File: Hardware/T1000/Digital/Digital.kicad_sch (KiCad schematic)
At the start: 71 parts, among them J1 Conn_01x02_Pin, J2 Conn_01x06_Socket, J3 Conn_01x04_Pin, J4 FTSH-107-01-L-DV-K-A, J5 USB_C_Receptacle_USB2.0, SW1 SW_SPDT, SW2 SW_SPDT, U1 MS5607-02BA, U2 MIA-M10Q, U3 STM32L422TBYx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

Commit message: V0 changes before order
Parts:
- removed BT1: 1S, Connector_JST:JST_PH_S2B-PH-K_1x02_P2.00mm_Horizontal, symbol Device:Battery_Cell
- removed C16, C17, C21: 1uF, Capacitor_SMD:C_0603_1608Metric, symbol Device:C_Small
- removed C18, C22, C23: 10uF, Capacitor_SMD:C_0805_2012Metric, symbol Device:C_Small
- removed C19: 2.2pF, Capacitor_SMD:C_0402_1005Metric, symbol Device:C_Small
- removed C20: 15uF, Capacitor_SMD:C_1206_3216Metric, symbol Device:C_Small
- removed D2: LED_Small, LED_SMD:LED_0603_1608Metric, symbol Device:LED_Small
- removed L1: 1uH, Inductor_SMD:L_0805_2012Metric, symbol Device:L_Small
- removed L2: 3.3uH, Inductor_SMD:L_1210_3225Metric, symbol Device:L_Small
- removed R11: 100m, Resistor_SMD:R_0402_1005Metric, symbol Device:R_Small
- removed R12: 10k, Resistor_SMD:R_0402_1005Metric, symbol Device:R_Small
- removed R13: 649k, Resistor_SMD:R_0402_1005Metric, symbol Device:R_Small
- removed R14: 294k, Resistor_SMD:R_0402_1005Metric, symbol Device:R_Small
- removed R15, R20: ??, Resistor_SMD:R_0402_1005Metric, symbol Device:R_Small
- removed R16, R19: 100k, Resistor_SMD:R_0402_1005Metric, symbol Device:R_Small
- removed R17: 113k, Resistor_SMD:R_0402_1005Metric, symbol Device:R_Small
- removed R18: 0, Resistor_SMD:R_0402_1005Metric, symbol Device:R_Small
- removed TP3: TestPoint, TestPoint:TestPoint_Pad_D1.0mm, symbol Connector:TestPoint
- removed U5: MIC5504-3.3YM5, Package_TO_SOT_SMD:SOT-23-5, symbol Regulator_Linear:MIC5504-3.3YM5
- removed U6: LM66200DRLR, BPP_Lib:SOT-5X3_DRL_TEX, symbol BPP_Lib:LM66200DRLR
- removed U7: LTC4065EDC-TRMPBF, BPP_Lib:DFN-6_DC_LIT, symbol BPP_Lib:LTC4065AEDC-TRMPBF
- removed U8: LTC3306CACBZ-R7, BPP_Lib:CB-6-19_ADI, symbol BPP_Lib:LTC3306CACBZ-R7
- added H1, H2: MountingHole, MountingHole:MountingHole_2.2mm_M2, symbol Mechanical:MountingHole
- added R24: 51k, Resistor_SMD:R_0402_1005Metric, symbol Device:R_Small
- J1: footprint Connector_PinHeader_1.00mm:PinHeader_1x02_P1.00mm_Vertical -> Connector_PinHeader_2.54mm:PinHeader_1x02_P2.54mm_Vertical
- Y2: value Crystal_Small -> 32.768k
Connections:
- net COMP1_INP: now also R24.2
- net VDD: now also R24.1
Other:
- added sheet Power (power.kicad_sch)
- note added: "Cutdown -> COMP1 is open drain, so pull up required"
- note removed: "1.8V SMPS"
- note removed: "3.3V SMPS"
- note removed: "Battery Charger"
- note removed: "Ideal Diode OR"
- company: (none) -> UMDBPP
- title: (none) -> T1000 - Digital & RF
- moved on the sheet: C15, J2, J3, J4, R8

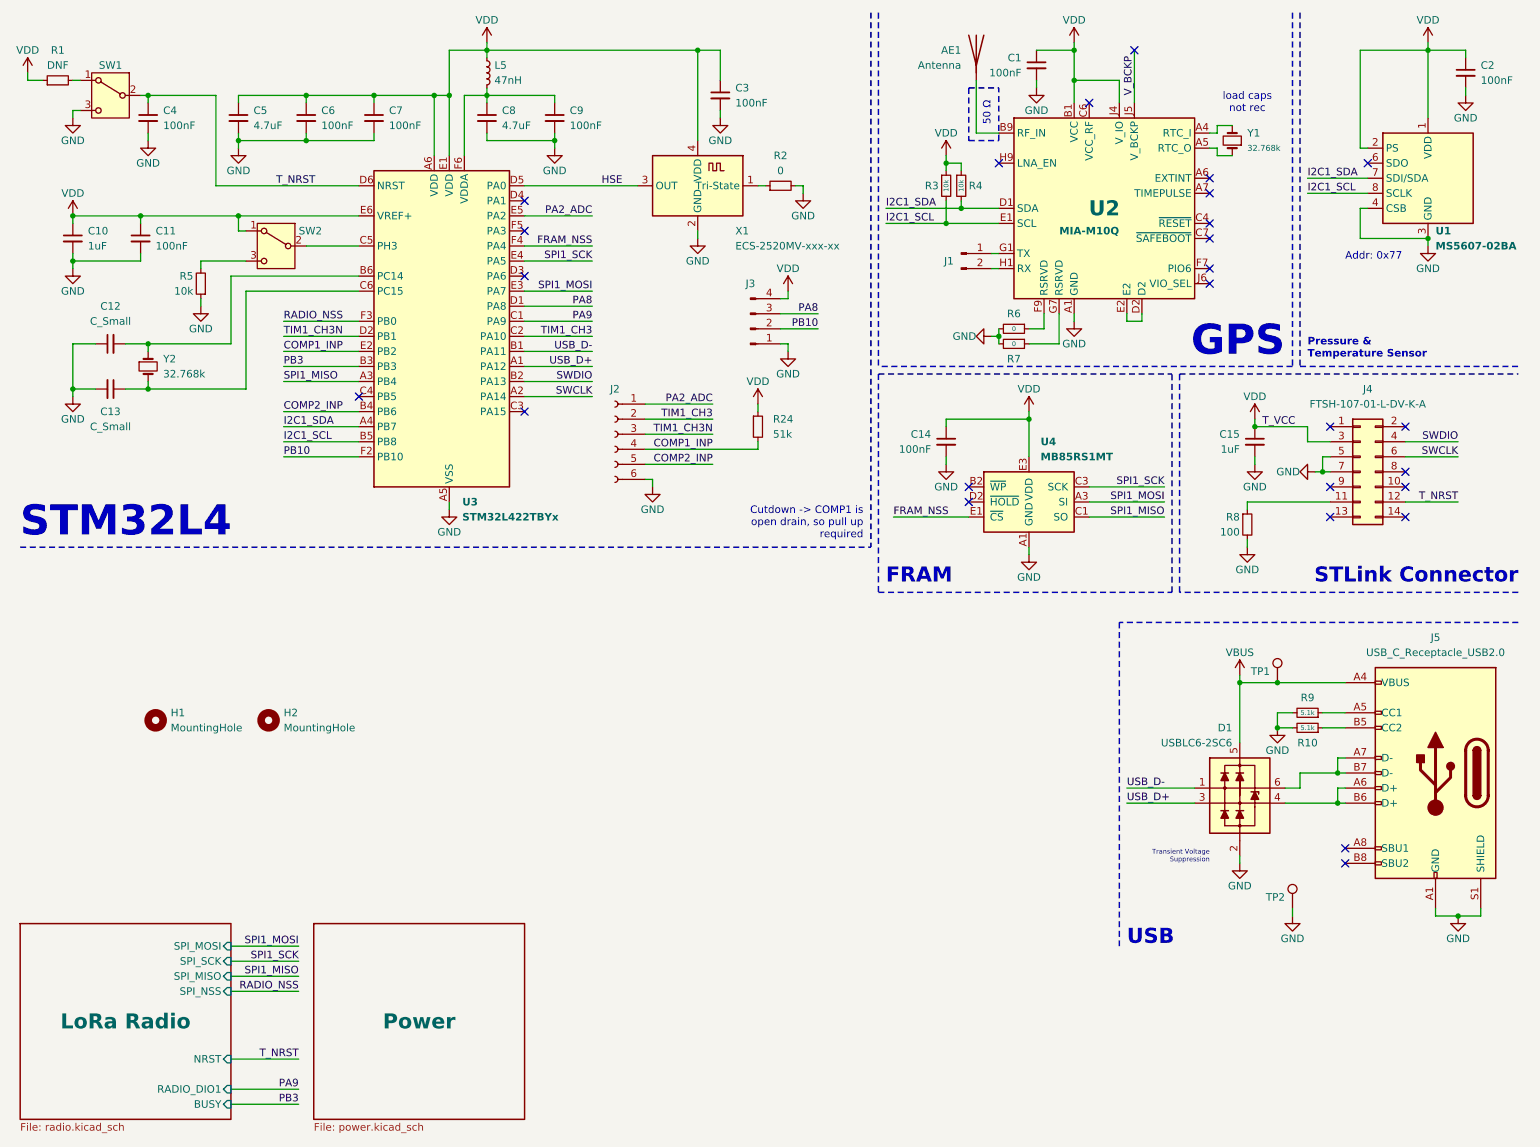
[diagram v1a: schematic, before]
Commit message: started STM32 package change (T1001)
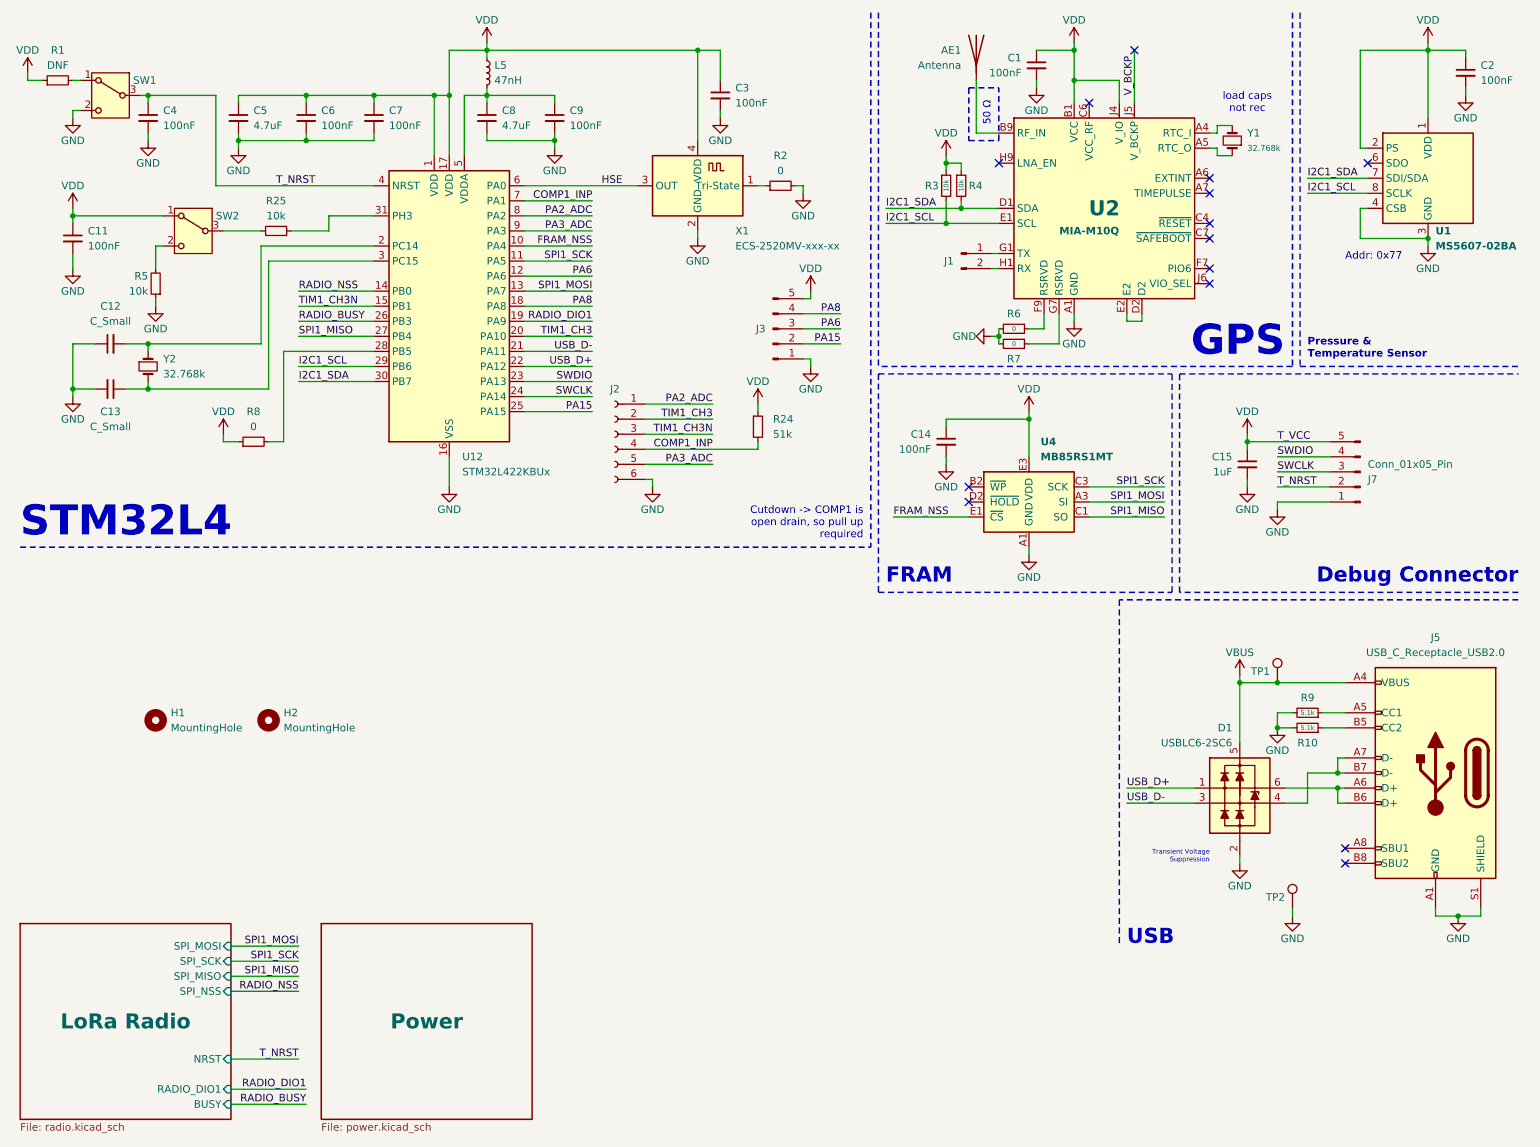
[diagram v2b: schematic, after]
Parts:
- removed C10: 1uF, Capacitor_SMD:C_0603_1608Metric, symbol Device:C_Small
- removed J3: Conn_01x04_Pin, Connector_PinHeader_2.54mm:PinHeader_1x04_P2.54mm_Vertical, symbol Connector:Conn_01x04_Pin
- removed J4: FTSH-107-01-L-DV-K-A, Connector_Samtec:CON14_2X7_DUK_FTSH_SAI-L, symbol Connector_Generic:Conn_02x07_Odd_Even
- removed U3: STM32L422TBYx, Package_CSP:ST_WLCSP-36_2.58x3.07mm_Layout6x6_P0.4mm, symbol MCU_ST_STM32L4:STM32L422TBYx
- added J3, J7: Conn_01x05_Pin, Connector_PinHeader_2.54mm:PinHeader_1x05_P2.54mm_Vertical, symbol Connector:Conn_01x05_Pin
- added R25: 10k, Resistor_SMD:R_0402_1005Metric, symbol Device:R_Small
- added U12: STM32L422KBUx, Package_DFN_QFN:QFN-32-1EP_5x5mm_P0.5mm_EP3.45x3.45mm, symbol MCU_ST_STM32L4:STM32L422KBUx
- R8: value 100 -> 0
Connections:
- net COMP1_INP: now also U12.7 (PA1)
- net FRAM_NSS: now also U12.10 (PA4)
- net GND: now also SW1.2 (B), J3.1 (Pin_1), J7.1 (Pin_1), U12.16 (VSS), U12.32 (VSS), U12.33 (VSS); no longer R8.2, SW1.3 (C)
- net HSE: now also U12.6 (PA0)
- net I2C1_SCL: now also U12.29 (PB6)
- net I2C1_SDA: now also U12.30 (PB7)
- net PA2_ADC: now also U12.8 (PA2)
- net PA8: now also J3.4 (Pin_4), U12.18 (PA8)
- net RADIO_NSS: now also U12.14 (PB0)
- net SPI1_MISO: now also U12.27 (PB4)
- net SPI1_MOSI: now also U12.13 (PA7)
- net SPI1_SCK: now also U12.11 (PA5)
- net SWCLK: now also J7.3 (Pin_3), U12.24 (PA14)
- net SWDIO: now also J7.4 (Pin_4), U12.23 (PA13)
- net TIM1_CH3: now also U12.20 (PA10)
- net TIM1_CH3N: now also U12.15 (PB1)
- net T_NRST: now also SW1.3 (C), J7.2 (Pin_2), U12.4 (NRST); no longer SW1.2 (B)
- net USB_D+: now also D1.1 (L1), U12.22 (PA12); no longer D1.3 (L2)
- net USB_D-: now also D1.3 (L2), U12.21 (PA11); no longer D1.1 (L1)
- net VDD: now also R8.1, J3.5 (Pin_5), J7.5 (Pin_5), U12.1 (VDD), U12.17 (VDD)
- net at SW2.2 (B): now also R5.2
- net at SW2.3 (C): now also R25.1; no longer R5.2
- net at C12.2, Y2.1: now also U12.2 (PC14)
- net at C13.1, Y2.2: now also U12.3 (PC15)
- net at C8.1, C9.1, L5.2: now also U12.5 (VDDA)
- net at J5.A6 (D+), J5.B6 (D+): now also D1.6 (L1); no longer D1.4 (L2)
- net at J5.A7 (D-), J5.B7 (D-): now also D1.4 (L2); no longer D1.6 (L1)
- net COMP2_INP renamed PA3_ADC
- net PA3_ADC: now also U12.9 (PA3)
- new net: R8.2, U12.28 (PB5)
- new net: R25.2, U12.31 (PH3)
- new net PA15: J3.2 (Pin_2), U12.25 (PA15)
- new net PA6: J3.3 (Pin_3), U12.12 (PA6)
- new net RADIO_BUSY: U12.26 (PB3)
- new net RADIO_DIO1: U12.19 (PA9)
- no-connect marks 26 -> 14
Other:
- note added: "Debug Connector"
- note removed: "STLink Connector"
- moved on the sheet: C11, C15, R5, SW2

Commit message: ordered T1001
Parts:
- removed R5: 10k, Resistor_SMD:R_0402_1005Metric, symbol Device:R_Small
- removed R8: 0, Resistor_SMD:R_0402_1005Metric, symbol Device:R_Small
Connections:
- net GND: now also SW2.2 (B)
- net VDD: now also U12.28 (PB5)
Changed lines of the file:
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@@
 	(wire
 		(pts
-			(xy 36.83 60.96) (xy 36.83 62.23)
-		)
-		(stroke
-			(width 0)
-			(type default)
-		)
-	)
-	(wire
-		(pts
 			(xy 92.71 17.78) (xy 92.71 19.05)
 		)
@@
 	(wire
 		(pts
-			(xy 48.26 85.09) (xy 50.8 85.09)
+			(xy 48.26 85.09) (xy 58.42 85.09)
 		)
 		(stroke
@@
 		)
 	)
-	(wire
-		(pts
-			(xy 55.88 85.09) (xy 58.42 85.09)
-		)
-		(stroke
-			(width 0)
-			(type default)
-		)
-	)
 	(polyline
 		(pts
@@
 	(wire
 		(pts
-			(xy 36.83 55.88) (xy 36.83 52.07)
+			(xy 36.83 52.07) (xy 36.83 55.88)
 		)
 		(stroke
@@
 	)
 	(symbol
-		(lib_id "Device:R_Small")
-		(at 53.34 85.09 90)
-		(unit 1)
-		(exclude_from_sim no)
-		(in_bom yes)
-		(on_board yes)
-		(dnp no)
-		(fields_autoplaced yes)
-		(property "Reference" "R8"
-			(at 53.34 80.01 90)
-			(effects
-				(font
-					(size 1.27 1.27)
-				)
-			)
-		)
-		(property "Value" "0"
-			(at 53.34 82.55 90)
-			(effects
-				(font
-					(size 1.27 1.27)
-				)
-			)
-		)
-		(property "Footprint" "Resistor_SMD:R_0402_1005Metric"
-			(at 53.34 85.09 0)
-			(effects
-				(font
-					(size 1.27 1.27)
-				)
-				(hide yes)
-			)
-		)
-		(property "Datasheet" "~"
-			(at 53.34 85.09 0)
-			(effects
-				(font
-					(size 1.27 1.27)
-				)
-				(hide yes)
-			)
-		)
-		(property "Description" "Resistor, small symbol"
-			(at 53.34 85.09 0)
-			(effects
-				(font
-					(size 1.27 1.27)
-				)
-				(hide yes)
-			)
-		)
-		(pin "2"
-		)
-		(pin "1"
-		)
-		(instances
-			(project "Digital"
-				(path "/14eb5cc5-1068-4dbf-9d6e-49ddc6215ab5"
-					(reference "R8")
-					(unit 1)
-				)
-			)
-		)
-	)
-	(symbol
 		(lib_id "Mechanical:MountingHole")
 		(at 36.83 132.08 0)
@@
 	(symbol
 		(lib_id "power:GND")
-		(at 36.83 62.23 0)
+		(at 36.83 55.88 0)
 		(unit 1)
 		(exclude_from_sim no)
@@
 		(dnp no)
 		(property "Reference" "#PWR018"
-			(at 36.83 68.58 0)
+			(at 36.83 62.23 0)
 			(effects
 				(font
@@
 		)
 		(property "Value" "GND"
-			(at 36.83 66.04 0)
+			(at 36.83 59.69 0)
 			(effects
 				(font
@@
 		)
 		(property "Footprint" ""
-			(at 36.83 62.23 0)
+			(at 36.83 55.88 0)
 			(effects
 				(font
@@
 		)
 		(property "Datasheet" ""
-			(at 36.83 62.23 0)
+			(at 36.83 55.88 0)
 			(effects
 				(font
@@
 		)
 		(property "Description" "Power symbol creates a global label with name \"GND\" , ground"
-			(at 36.83 62.23 0)
+			(at 36.83 55.88 0)
 			(effects
 				(font
@@
 					(unit 1)
 				)
-			)
-		)
-	)
-	(symbol
-		(lib_id "Device:R_Small")
-		(at 36.83 58.42 180)
-		(unit 1)
-		(exclude_from_sim no)
-		(in_bom yes)
-		(on_board yes)
-		(dnp no)
-		(property "Reference" "R5"
-			(at 35.56 57.15 0)
-			(effects
-				(font
-					(size 1.27 1.27)
-				)
-				(justify left)
-			)
-		)
-		(property "Value" "10k"
-			(at 35.56 59.69 0)
-			(effects
-				(font
-					(size 1.27 1.27)
-				)
-				(justify left)
-			)
-		)
-		(property "Footprint" "Resistor_SMD:R_0402_1005Metric"
-			(at 36.83 58.42 0)
-			(effects
-				(font
-					(size 1.27 1.27)
-				)
-				(hide yes)
-			)
-		)
-		(property "Datasheet" "~"
-			(at 36.83 58.42 0)
-			(effects
-				(font
-					(size 1.27 1.27)
-				)
-				(hide yes)
-			)
-		)
-		(property "Description" "Resistor, small symbol"
-			(at 36.83 58.42 0)
-			(effects
-				(font
-					(size 1.27 1.27)
-				)
-				(hide yes)
-			)
-		)
-		(pin "1"
-		)
-		(pin "2"
-		)
-		(instances
-			(project "Digital"
-				(path "/14eb5cc5-1068-4dbf-9d6e-49ddc6215ab5"
-					(reference "R5")
-					(unit 1)
-				)
